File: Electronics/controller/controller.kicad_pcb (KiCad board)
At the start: 2 copper layers, 113 x 56.5 mm, 30 parts, among them P1 POWER, P2 PANEL_1, P3 PANEL_2, Q1 FET, SW1 SW_PUSH, U1 LM317T, U2 74HC595, U3 Arduino_Pro_Micro

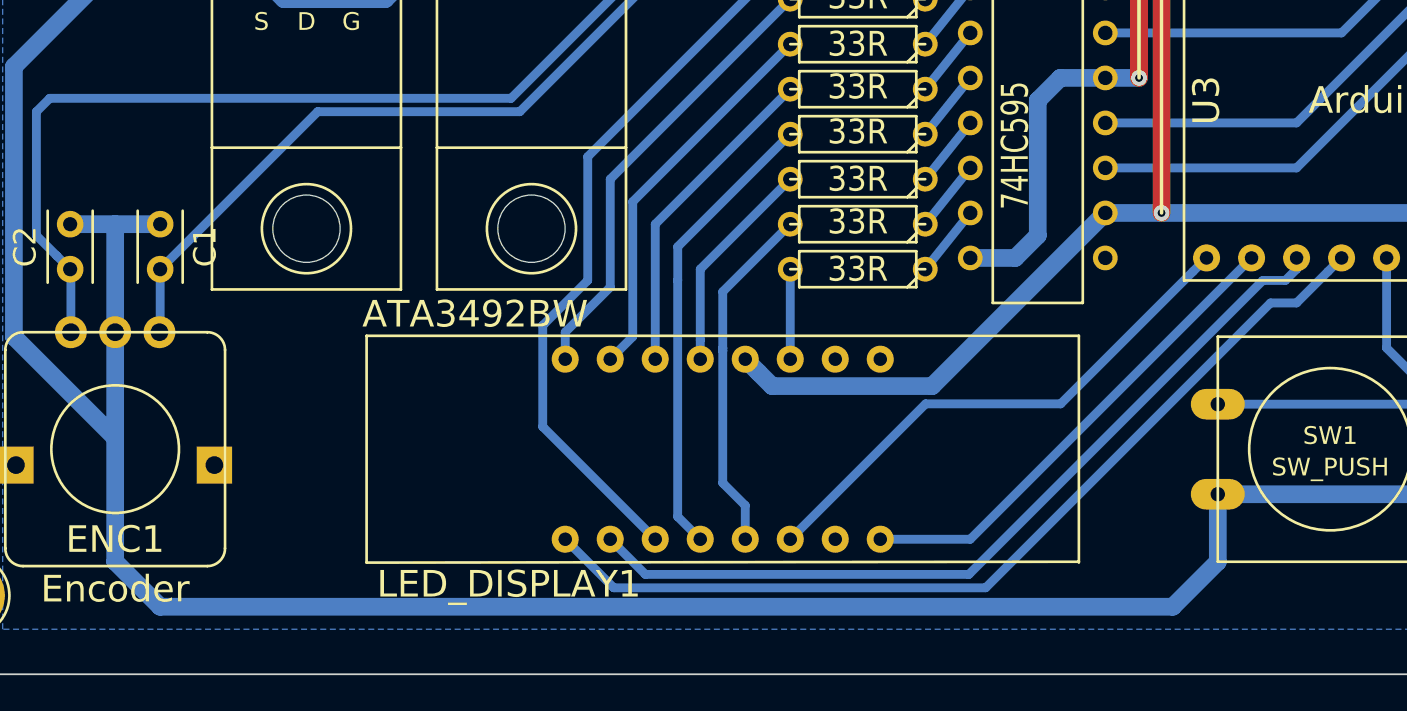
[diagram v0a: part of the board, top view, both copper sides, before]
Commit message: Fixed some bad pinouts on the 7-seg.
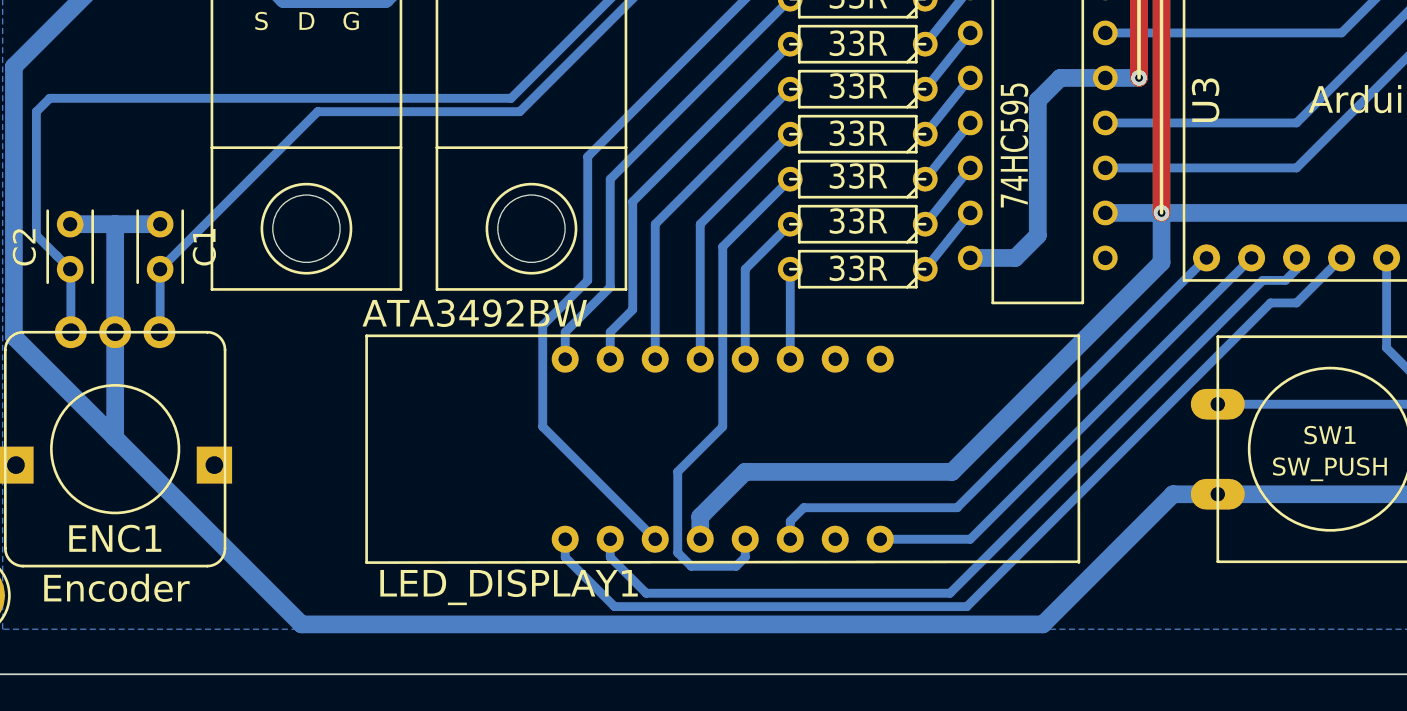
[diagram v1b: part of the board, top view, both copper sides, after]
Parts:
- moved R1 5.08 mm to (108.0, 86.4)
- moved R9 2.54 mm to (108.0, 83.8)
- moved R7 2.54 mm to (108.0, 81.3)
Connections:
- LED_DISPLAY1 pad 12: VCC -> Net-(LED_DISPLAY1-Pad12)
- LED_DISPLAY1 pad 4: Net-(LED_DISPLAY1-Pad4) -> VCC
- R1 pad 1: /COL -> /E
- R1 pad 2: Net-(LED_DISPLAY1-Pad4) -> Net-(LED_DISPLAY1-Pad12)
- R7 pad 1: /C -> /COL
- R9 pad 1: /E -> /C
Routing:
- net Net-(LED_DISPLAY1-Pad4): track 26.0 -> 0.00 mm
- net VCC: track 120.1 -> 131.1 mm
- net Net-(LED_DISPLAY1-Pad5): track 19.9 -> 29.1 mm
- net Net-(LED_DISPLAY1-Pad12): track 0.00 -> 8.93 mm
- net GND: track 295.6 -> 290.1 mm
- net Net-(LED_DISPLAY1-Pad13): track 12.3 -> 14.8 mm
- net /D14: track 47.3 -> 48.8 mm
- net /D15: track 52.7 -> 54.1 mm
- net /D10: track 30.1 -> 30.7 mm

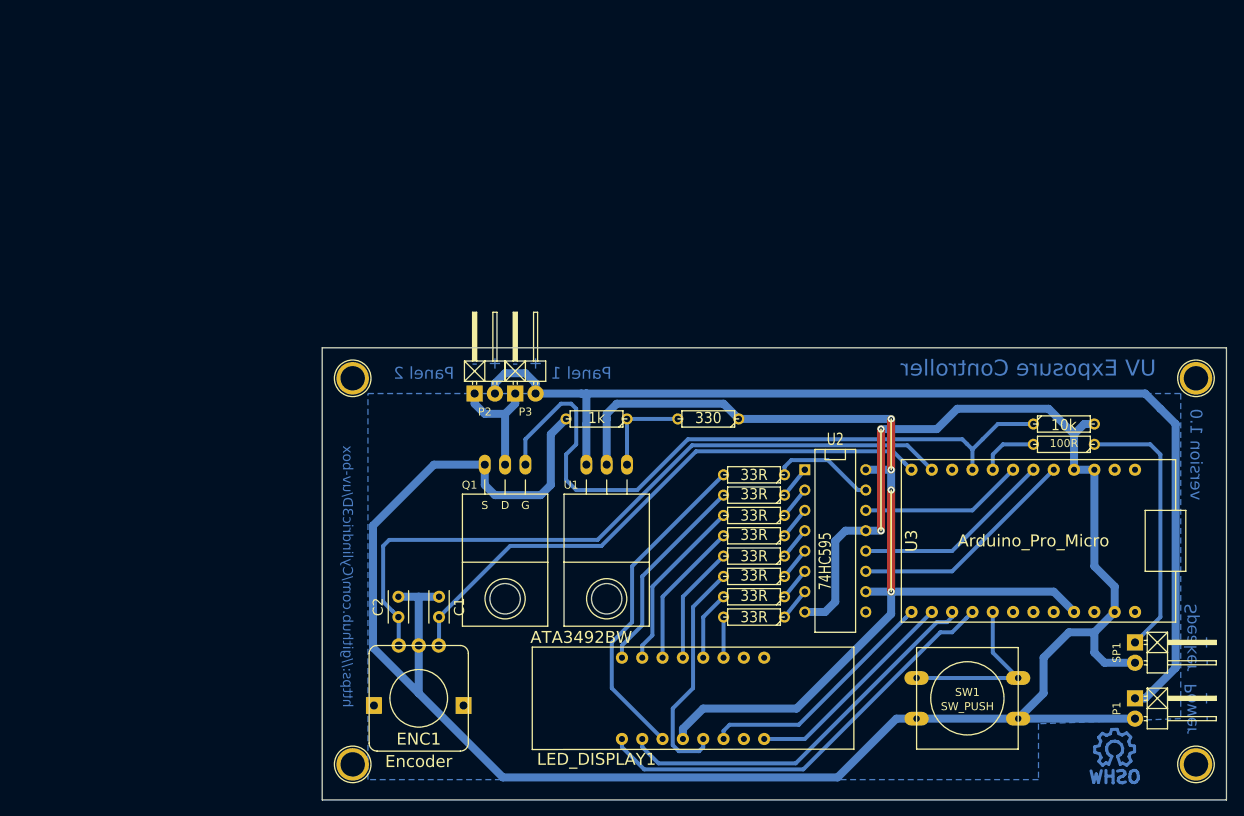
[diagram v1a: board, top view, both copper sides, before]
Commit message: Updated schematics after prototype testing.
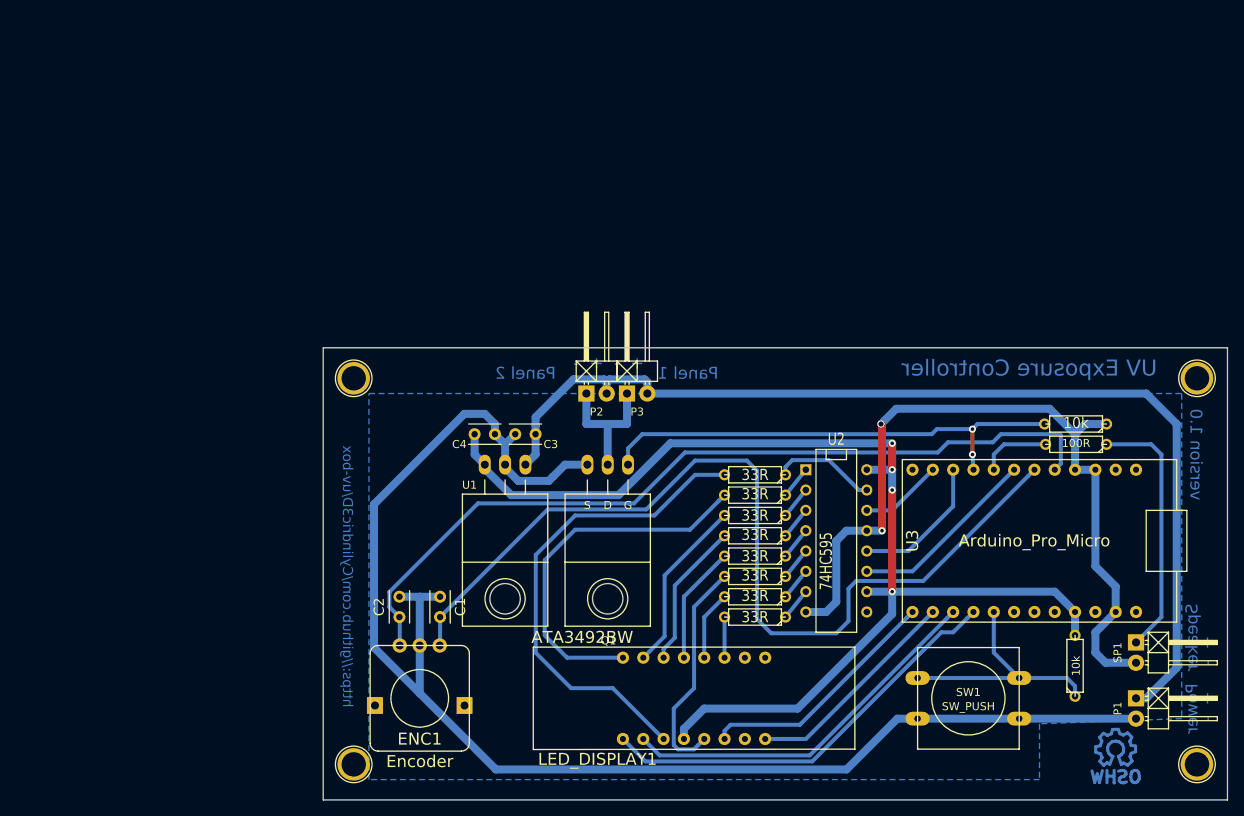
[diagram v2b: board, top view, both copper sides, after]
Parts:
- removed R3: 330, Discret:R3
- added C3: 0.33µF, Capacitors_ThroughHole:Capacitor4x3RM2.5, F.Cu at (80.6, 66.0)
- added C4: 0.1µF, Capacitors_ThroughHole:Capacitor4x3RM2.5, F.Cu at (73.0, 66.0)
- C1, C2: value 0.1uF -> 0.1µF
- Q1: value FET -> P55NF
- R2: value 1k -> 10k
- U1: value LM317T -> LM7805CT
- moved R2 67.3 mm to (148.1, 95.0), turned to 90 degrees
- moved P2 14.0 mm to (88.3, 61.0)
- moved P3 14.0 mm to (93.3, 61.0)
- moved Q1 12.8 mm to (89.7, 69.8)
- moved U1 12.7 mm to (76.8, 69.8)
- moved R12 1.52 mm to (148.2, 67.3)
- moved R4 1.52 mm to (148.2, 64.8), turned to 180 degrees
- moved 1pin 0.13 mm to (163.3, 59.1)
- moved 1pin 0.13 mm to (163.3, 107.3)
- moved P1 0.13 mm to (155.7, 100.3)
- moved SP1 0.13 mm to (155.7, 93.3)
- moved SW1 0.13 mm to (134.7, 99.1)
- moved Symbol_OSHW-Logo_CopperTop 0.13 mm to (153.2, 105.4)
- moved U3 0.13 mm to (150.6, 80.6)
- moved 1pin 0.13 mm to (57.9, 59.1)
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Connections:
- net /D5 renamed /PWM5
- C1 pad 1: /D9 -> /D3
- C2 pad 2: /D8 -> /D2
- ENC1 pad A: /D9 -> /D3
- ENC1 pad B: /D8 -> /D2
- R2 pad 1: Net-(R2-Pad1) -> /A0
- R2 pad 2: GND -> VCC
- R4 pad 1: /D6 -> GND
- R4 pad 2: GND -> /D6
- U1 pad 1: Net-(R2-Pad1) -> +12V
- U1 pad 2: VCC -> GND
- U1 pad 3: +12V -> VCC
- U2 pad 11: /D2 -> /D4
- U2 pad 12: /D3 -> /D7
- U2 pad 14: /D4 -> /D8
- U3 pad 10: (no net) -> /D7
- U3 pad 12: /D9 -> (no net)
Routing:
- net /D3: track 25.2 -> 116.7 mm
- net /D8: track 88.4 -> 10.4 mm
- net /D2: track 28.8 -> 104.1 mm
- net /D9: track 72.2 -> 0.00 mm
- net /D6: track 87.6 -> 61.7 mm, vias 0 -> 2
- net Net-(LED_DISPLAY1-Pad16): track 25.6 -> 46.2 mm
- net Net-(LED_DISPLAY1-Pad3): track 41.4 -> 60.4 mm
- net /D7: track 0.00 -> 17.7 mm
- net VCC: track 131.1 -> 147.7 mm
- net Net-(R2-Pad1): track 12.1 -> 0.00 mm
- net GND: track 290.1 -> 279.5 mm
- net /A0: track 22.9 -> 30.9 mm
- net +12V: track 136.3 -> 130.6 mm
- net /D4: track 20.5 -> 23.7 mm
- net /12VGND: track 15.0 -> 18.0 mm
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
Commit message: Moved some parts around on the board.
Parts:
- moved Symbol_OSHW-Logo_CopperTop 58.2 mm to (110.4, 65.9)
- moved R12 56.0 mm to (108.5, 27.8)
- moved R4 56.0 mm to (108.5, 25.3)
- moved SW1 55.1 mm to (96.4, 59.6)
- moved U3 55.1 mm to (112.3, 41.1)
- moved C1 55.1 mm to (30.4, 49.4)
- moved C3 55.1 mm to (42.3, 26.5)
- moved C4 55.1 mm to (34.7, 26.5)
- moved Q1 55.1 mm to (51.3, 30.4)
- moved R10 55.1 mm to (69.7, 49.4)
- moved 1pin 55.1 mm to (125.0, 19.6)
- moved 1pin 55.1 mm to (125.0, 67.8)
- moved 1pin 55.1 mm to (19.6, 19.6)
- moved 1pin 55.1 mm to (19.6, 67.8)
- moved C2 55.1 mm to (25.3, 46.9)
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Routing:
- net /D3: track 116.7 -> 123.7 mm
- net /D4: track 23.7 -> 29.9 mm
- net +12V: track 130.6 -> 134.8 mm
- net /12VGND: track 18.0 -> 14.0 mm
- net GND: track 279.5 -> 275.8 mm
- net Net-(LED_DISPLAY1-Pad3): track 60.4 -> 63.3 mm
- net /D7: track 17.7 -> 20.1 mm
- net /D2: track 104.1 -> 102.3 mm
- net Net-(LED_DISPLAY1-Pad14): track 18.4 -> 20.0 mm
- net Net-(LED_DISPLAY1-Pad13): track 14.8 -> 16.4 mm
- net Net-(LED_DISPLAY1-Pad15): track 22.0 -> 23.6 mm
- net Net-(LED_DISPLAY1-Pad5): track 28.3 -> 29.8 mm
- net /PWM5: track 8.91 -> 7.51 mm
- net /D8: track 10.4 -> 11.4 mm
- net /D15: track 52.7 -> 53.5 mm
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
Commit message: Tidied up some visual layout issues.
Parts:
- SP1: value SPEAKER -> PIEZO
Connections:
- net /A0 renamed /D18

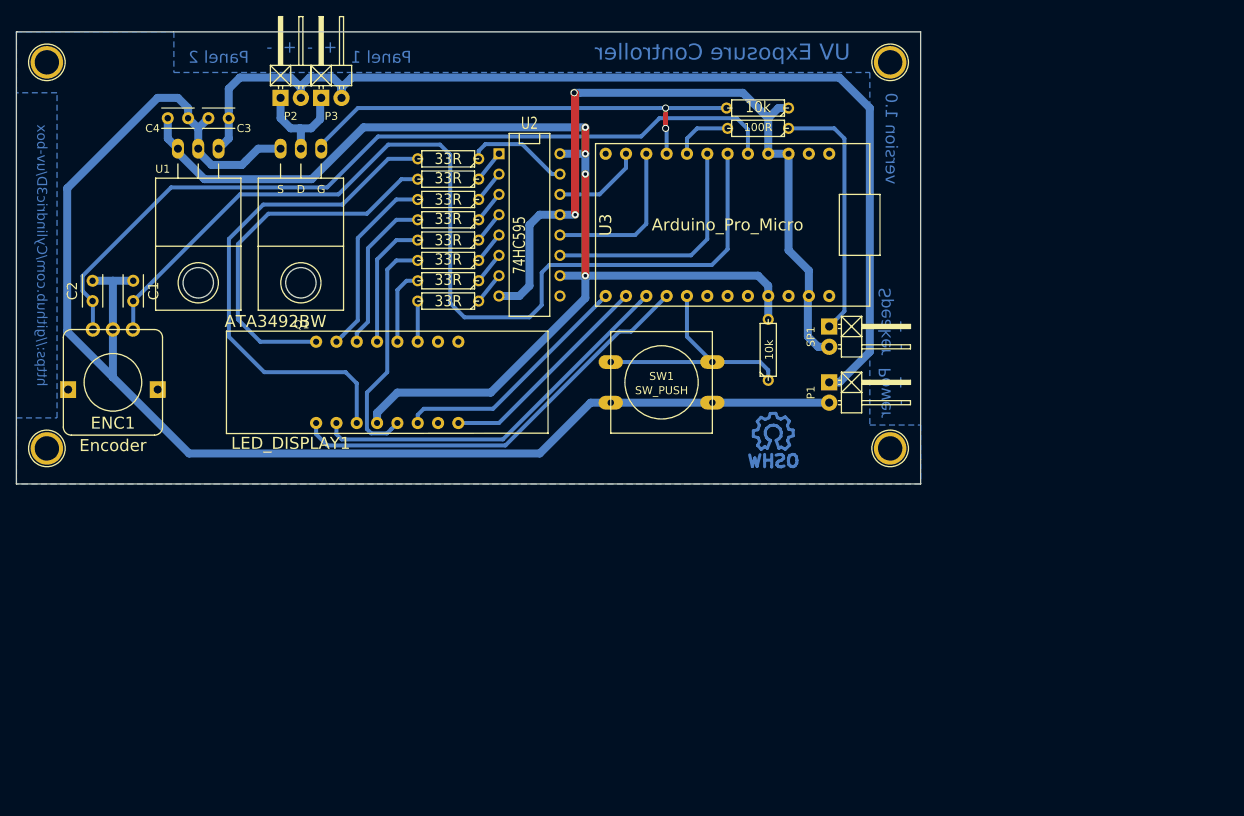
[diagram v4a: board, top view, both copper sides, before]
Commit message: Added some plots for the v1 controller board.
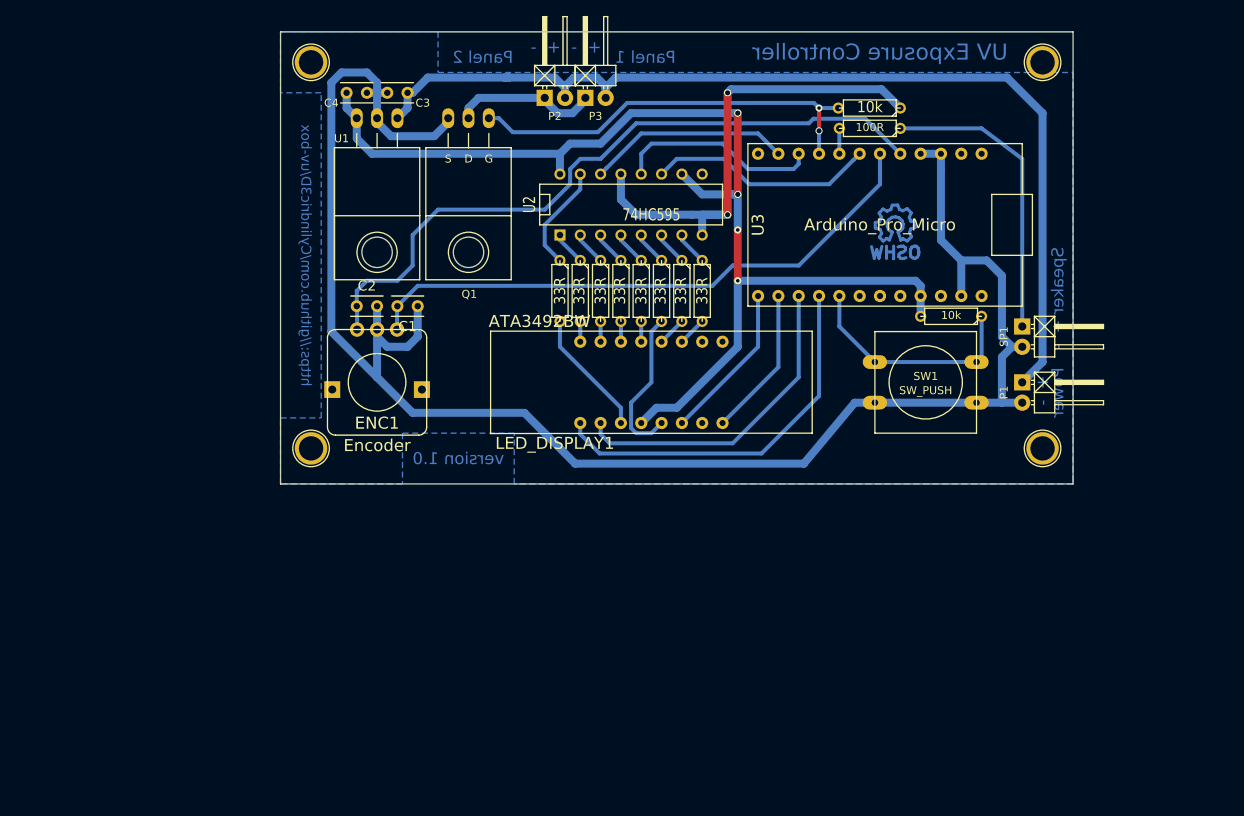
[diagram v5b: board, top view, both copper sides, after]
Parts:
- moved C2 35.7 mm to (60.8, 50.0), turned to 180 degrees
- moved C1 33.0 mm to (63.4, 50.0), turned to 0 degrees
- moved P2 33.0 mm to (83.1, 24.0)
- moved SW1 33.0 mm to (129.4, 59.6)
- moved 1pin 33.0 mm to (52.6, 19.6)
- moved 1pin 33.0 mm to (52.6, 67.8)
- moved LED_DISPLAY1 33.0 mm to (95.1, 59.6)
- moved P3 33.0 mm to (88.1, 24.0)
- moved ENC1 33.0 mm to (60.8, 53.0)
- moved R10 31.8 mm to (101.5, 48.1), turned to 270 degrees
- moved Symbol_OSHW-Logo_CopperTop 30.2 mm to (125.6, 39.9)
- moved R1 29.2 mm to (98.9, 48.1), turned to 270 degrees
- moved R9 26.9 mm to (96.4, 48.1), turned to 270 degrees
- moved R7 25.0 mm to (93.9, 48.1), turned to 270 degrees
- moved P1 24.1 mm to (141.5, 60.8)
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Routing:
- net /D3: track 123.7 -> 73.4 mm
- net Net-(LED_DISPLAY1-Pad3): track 63.3 -> 15.9 mm
- net Net-(LED_DISPLAY1-Pad16): track 46.2 -> 2.54 mm
- net Net-(LED_DISPLAY1-Pad15): track 23.6 -> 2.54 mm
- net Net-(LED_DISPLAY1-Pad14): track 20.0 -> 2.54 mm
- net /D2: track 102.3 -> 86.9 mm
- net /D8: track 11.4 -> 25.4 mm
- net Net-(LED_DISPLAY1-Pad13): track 16.4 -> 2.54 mm
- net /D10: track 30.7 -> 19.8 mm
- net Net-(LED_DISPLAY1-Pad5): track 29.8 -> 19.5 mm
- net /D6: track 62.0 -> 52.1 mm
- net /D16: track 27.5 -> 18.8 mm
- net VCC: track 148.4 -> 140.0 mm
- net /D14: track 47.8 -> 40.2 mm
- net +12V: track 134.8 -> 128.4 mm
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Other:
- board size 113 x 56.5 mm -> 99.1 x 56.5 mm
